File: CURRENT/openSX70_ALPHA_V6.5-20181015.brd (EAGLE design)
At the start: 95.9 x 27.9 mm, 42 parts, among them J1 687106183722, Q1 5.8A/30V/35mΩ, Q2 5.8A/30V/35mΩ, U1 ATMEGA328P_TQFP, Y1 CSTCE8M00G52Z-R0

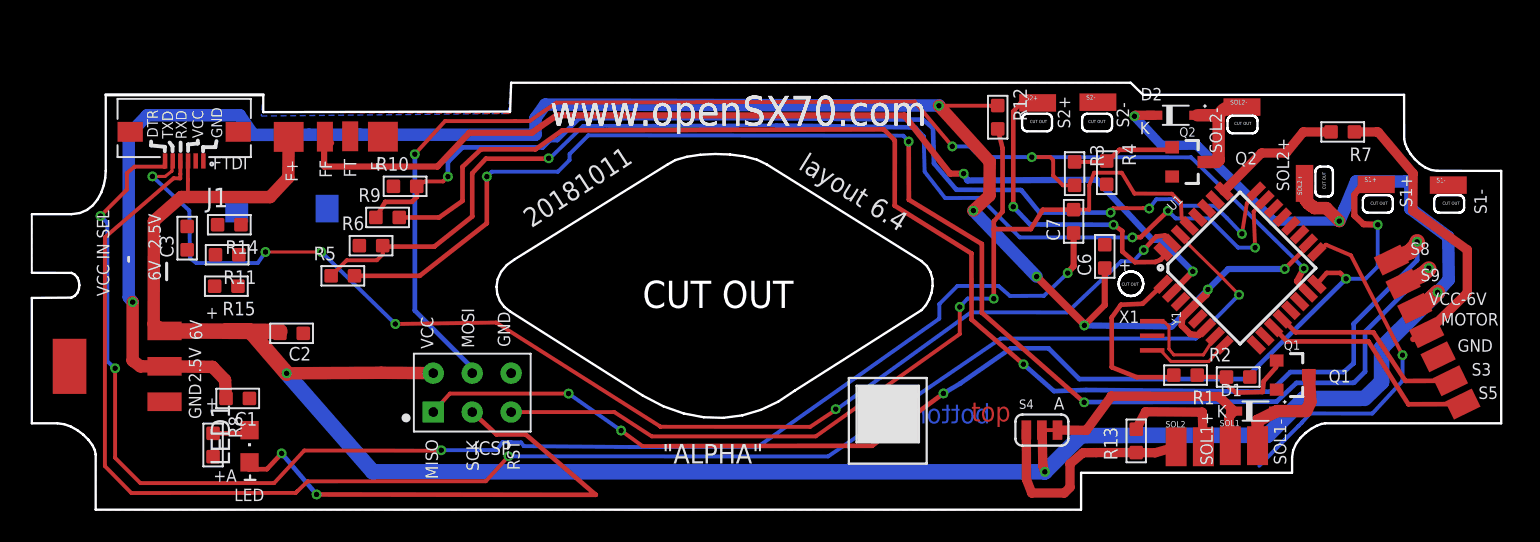
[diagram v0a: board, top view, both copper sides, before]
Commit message: New layout 6.5 with new flexcable custom connector
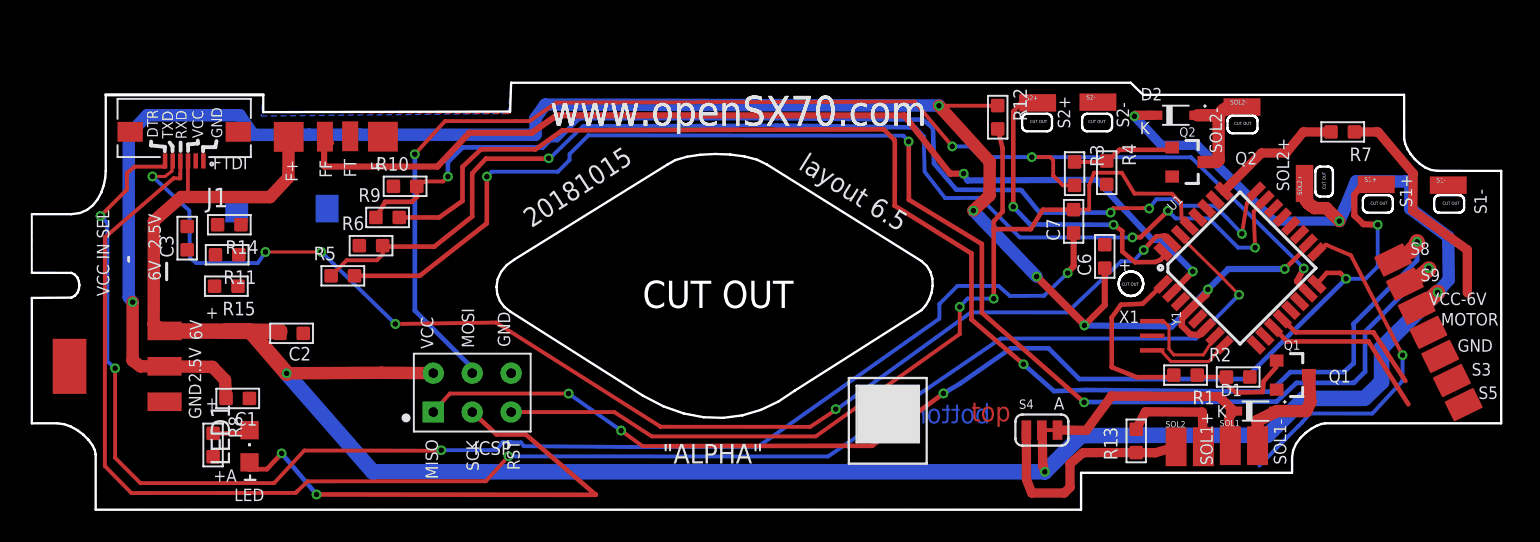
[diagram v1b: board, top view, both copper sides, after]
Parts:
- removed U$1: SX70-7-PAD, openSX70:SX70-7-PAD
- added U$3: SX70-7-PAD, _openSX70:SX70-7-PAD-PROPER
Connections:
- net 6V: now also U$3.VCC; no longer U$1.VCC-6V
- net GND: now also U$3.GND; no longer U$1.GND
- net MOTOR-HEADER: now also U$3.MOTOR; no longer U$1.MOTOR+
- net S3: now also U$3.S3; no longer U$1.S3
- net S5: now also U$3.S5; no longer U$1.S5
- net S8@6V: now also U$3.S8; no longer U$1.S8
- net S9@6V: now also U$3.S9; no longer U$1.S9
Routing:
- net MOTOR-HEADER: track 19.4 -> 14.7 mm
- net S5: track 15.8 -> 11.4 mm
- net S3: track 13.0 -> 10.1 mm
- net S9@6V: track 94.3 -> 92.9 mm
- net S8@6V: track 89.7 -> 88.4 mm
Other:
- board text added: "20181015"
- board text added: "layout 6.5"
- board text added: "openSX70 project visit www.openSX70.com version 6.5 "ALPHA" 20181015 by Joaquín de Prada"
- board text removed: "20181011"
- board text removed: "layout 6.4"
- board text removed: "openSX70 project visit www.openSX70.com version 6.4 "ALPHA" 20181011 by Joaquín de Prada"

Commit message: adding to the board
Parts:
- added LED2: DUAL-LED-3MM-NO-HOLE, _openSX70:DUOLED-A-3MM
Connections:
- new net LED2: LED2.ANODE-GREEN, U1.9
- net LED: now also LED2.ANODE-RED
- net N$5: now also LED2.COMMON-CATODE
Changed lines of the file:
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@@
 <grid distance="0.005" unitdist="mm" unit="mm" style="lines" multiple="1" display="yes" altdistance="0.0005" altunitdist="mm" altunit="mm"/>
 <layers>
-<layer number="1" name="Top" color="4" fill="1" visible="yes" active="yes"/>
+<layer number="1" name="Top" color="4" fill="1" visible="no" active="yes"/>
 <layer number="2" name="Route2" color="1" fill="3" visible="no" active="no"/>
 <layer number="3" name="Route3" color="4" fill="3" visible="no" active="no"/>
@@
 <layer number="19" name="Unrouted" color="6" fill="1" visible="yes" active="yes"/>
 <layer number="20" name="Dimension" color="24" fill="1" visible="yes" active="yes"/>
-<layer number="21" name="tPlace" color="7" fill="1" visible="yes" active="yes"/>
+<layer number="21" name="tPlace" color="7" fill="1" visible="no" active="yes"/>
 <layer number="22" name="bPlace" color="7" fill="1" visible="yes" active="yes"/>
-<layer number="23" name="tOrigins" color="15" fill="1" visible="yes" active="yes"/>
+<layer number="23" name="tOrigins" color="15" fill="1" visible="no" active="yes"/>
 <layer number="24" name="bOrigins" color="15" fill="1" visible="yes" active="yes"/>
-<layer number="25" name="tNames" color="7" fill="1" visible="yes" active="yes"/>
+<layer number="25" name="tNames" color="7" fill="1" visible="no" active="yes"/>
 <layer number="26" name="bNames" color="7" fill="1" visible="yes" active="yes"/>
 <layer number="27" name="tValues" color="7" fill="1" visible="no" active="yes"/>
@@
 <layer number="37" name="tTest" color="7" fill="1" visible="no" active="yes"/>
 <layer number="38" name="bTest" color="7" fill="1" visible="no" active="yes"/>
-<layer number="39" name="tKeepout" color="4" fill="11" visible="yes" active="yes"/>
+<layer number="39" name="tKeepout" color="4" fill="11" visible="no" active="yes"/>
 <layer number="40" name="bKeepout" color="1" fill="11" visible="yes" active="yes"/>
-<layer number="41" name="tRestrict" color="4" fill="10" visible="yes" active="yes"/>
+<layer number="41" name="tRestrict" color="4" fill="10" visible="no" active="yes"/>
 <layer number="42" name="bRestrict" color="1" fill="10" visible="yes" active="yes"/>
 <layer number="43" name="vRestrict" color="2" fill="10" visible="no" active="yes"/>
-<layer number="44" name="Drills" color="7" fill="1" visible="yes" active="yes"/>
+<layer number="44" name="Drills" color="7" fill="1" visible="no" active="yes"/>
 <layer number="45" name="Holes" color="7" fill="1" visible="yes" active="yes"/>
 <layer number="46" name="Milling" color="3" fill="1" visible="no" active="yes"/>
@@
 <layer number="49" name="Reference" color="7" fill="1" visible="no" active="yes"/>
 <layer number="50" name="dxf" color="7" fill="1" visible="no" active="no"/>
-<layer number="51" name="tDocu" color="7" fill="1" visible="yes" active="yes"/>
+<layer number="51" name="tDocu" color="7" fill="1" visible="no" active="yes"/>
 <layer number="52" name="bDocu" color="7" fill="1" visible="yes" active="yes"/>
 <layer number="53" name="tGND_GNDA" color="7" fill="9" visible="no" active="no"/>
@@
 <element name="C1" library="Seeed-Capacitor" library_urn="urn:adsk.eagle:library:464" package="C0603" package3d_urn="urn:adsk.eagle:package:32378/1" value="10uf" x="15.494" y="8.0645" rot="R270">
 <attribute name="MPN" value="CC0603KRX5R6BB106" x="15.494" y="8.0645" size="1.778" layer="27" rot="R270" display="off"/>
+<attribute name="NAME" x="16.764" y="8.3185" size="0.635" layer="33" ratio="10" rot="R180"/>
 <attribute name="NAME" x="16.764" y="7.1755" size="0.889" layer="25" ratio="11" rot="R180"/>
-<attribute name="NAME" x="16.764" y="8.3185" size="0.635" layer="33" ratio="10" rot="R180"/>
 <attribute name="VALUE" x="16.764" y="9.652" size="0.635" layer="27" ratio="10" rot="R180"/>
 </element>
 <element name="C2" library="Seeed-Capacitor" library_urn="urn:adsk.eagle:library:464" package="C0603" package3d_urn="urn:adsk.eagle:package:32378/1" value="100nf" x="19.009" y="12.3135" rot="R270">
 <attribute name="MPN" value="CC0603KRX7R9BB104" x="19.009" y="12.3135" size="1.778" layer="27" rot="R270" display="off"/>
+<attribute name="NAME" x="20.279" y="12.5675" size="0.635" layer="33" ratio="10" rot="R180"/>
 <attribute name="NAME" x="20.279" y="11.4245" size="0.889" layer="25" ratio="11" rot="R180"/>
-<attribute name="NAME" x="20.279" y="12.5675" size="0.635" layer="33" ratio="10" rot="R180"/>
 <attribute name="VALUE" x="20.279" y="13.901" size="0.635" layer="27" ratio="10" rot="R180"/>
 </element>
 <element name="C6" library="Seeed-Capacitor" library_urn="urn:adsk.eagle:library:464" package="C0603" package3d_urn="urn:adsk.eagle:package:32378/1" value="100nf" x="72.0725" y="17.3355" rot="R180">
 <attribute name="MPN" value="CC0603KRX7R9BB104" x="72.0725" y="17.3355" size="1.778" layer="27" rot="R180" display="off"/>
+<attribute name="NAME" x="72.3265" y="16.0655" size="0.635" layer="33" ratio="10" rot="R90"/>
 <attribute name="NAME" x="71.1835" y="16.0655" size="0.889" layer="25" ratio="11" rot="R90"/>
-<attribute name="NAME" x="72.3265" y="16.0655" size="0.635" layer="33" ratio="10" rot="R90"/>
 <attribute name="VALUE" x="73.66" y="16.0655" size="0.635" layer="27" ratio="10" rot="R90"/>
 </element>
 <element name="C7" library="Seeed-Capacitor" library_urn="urn:adsk.eagle:library:464" package="C0603" package3d_urn="urn:adsk.eagle:package:32378/1" value="100nf" x="70.0405" y="19.6215" rot="R180">
 <attribute name="MPN" value="CC0603KRX7R9BB104" x="70.0405" y="19.6215" size="1.778" layer="27" rot="R180" display="off"/>
+<attribute name="NAME" x="70.2945" y="18.3515" size="0.635" layer="33" ratio="10" rot="R90"/>
 <attribute name="NAME" x="69.1515" y="18.3515" size="0.889" layer="25" ratio="11" rot="R90"/>
-<attribute name="NAME" x="70.2945" y="18.3515" size="0.635" layer="33" ratio="10" rot="R90"/>
 <attribute name="VALUE" x="71.628" y="18.3515" size="0.635" layer="27" ratio="10" rot="R90"/>
 </element>
@@
 <element name="C3" library="Seeed-Capacitor" library_urn="urn:adsk.eagle:library:464" package="C0603" package3d_urn="urn:adsk.eagle:package:32378/1" value="100nf" x="12.195" y="18.525" rot="R180">
 <attribute name="MPN" value="CC0603KRX7R9BB104" x="12.195" y="18.525" size="1.778" layer="27" rot="R180" display="off"/>
+<attribute name="NAME" x="12.449" y="17.255" size="0.635" layer="33" ratio="10" rot="R90"/>
 <attribute name="NAME" x="11.306" y="17.255" size="0.889" layer="25" ratio="11" rot="R90"/>
-<attribute name="NAME" x="12.449" y="17.255" size="0.635" layer="33" ratio="10" rot="R90"/>
 <attribute name="VALUE" x="13.7825" y="17.255" size="0.635" layer="27" ratio="10" rot="R90"/>
 </element>
@@
 </element>
 <element name="U$3" library="_openSX70" package="SX70-7-PAD-PROPER" value="SX70-7-PAD" x="89.23" y="17.261" rot="R296"/>
+<element name="LED2" library="_openSX70" package="DUOLED-A-3MM" package3d_urn="urn:adsk.eagle:package:15877/1" value="DUAL-LED-3MM-NO-HOLE" x="29.6" y="30.065" rot="MR180">
+<attribute name="NAME" x="33.41" y="27.525" size="1.27" layer="26" ratio="10" rot="MR180"/>
+<attribute name="VALUE" x="33.41" y="32.605" size="1.27" layer="28" ratio="10" rot="MR180"/>
+</element>
 </elements>
 <signals>
@@
 <wire x1="91.5035" y1="9.2075" x2="91.5035" y2="10.89025" width="0.254" layer="16"/>
 <via x="18.3618" y="4.4832" extent="1-16" drill="0.35"/>
+<contactref element="LED2" pad="ANODE-RED"/>
 <wire x1="38.861665625" y1="1.77511875" x2="82.1569" y2="3.6709" width="0" layer="19" extent="1-16"/>
+<wire x1="27.1" y1="30.065" x2="16.215" y2="3.435" width="0" layer="19" extent="1-1"/>
 </signal>
 <signal name="S3">
@@
 <contactref element="R8" pad="2"/>
 <contactref element="LED1" pad="C"/>
-<wire x1="13.885" y1="5.788" x2="15.15" y2="5.788" width="0.3048" layer="1"/>
-<wire x1="15.15" y1="5.788" x2="16.058" y2="5.788" width="0.3048" layer="1"/>
+<wire x1="13.885" y1="5.788" x2="16.058" y2="5.788" width="0.3048" layer="1"/>
 <wire x1="16.058" y1="5.788" x2="16.265" y2="5.995" width="0.3048" layer="1"/>
+<contactref element="LED2" pad="COMMON-CATODE"/>
+<wire x1="29.59" y1="30.065" x2="13.885" y2="5.788" width="0" layer="19" extent="1-1"/>
 </signal>
 <signal name="DTR">
@@
 <wire x1="15.707" y1="19.4" x2="83.085796875" y2="20.457353125" width="0" layer="19" extent="1-1"/>
 </signal>
+<signal name="LED2">
+<contactref element="LED2" pad="ANODE-GREEN"/>
+<contactref element="U1" pad="9"/>
+<wire x1="32.12" y1="30.065" x2="81.954425" y2="11.558271875" width="0" layer="19" extent="1-1"/>
+</signal>
 </signals>

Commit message: update
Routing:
- net S9@2.5V: track 75.7 -> 64.4 mm, vias 4 -> 3
- net S8@2.5V: track 69.5 -> 58.8 mm, vias 4 -> 3
- net S8@6V: track 88.4 -> 78.8 mm
- net S9@6V: track 92.9 -> 84.0 mm, vias 4 -> 3

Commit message: Work in progress
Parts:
- moved LED2 5.34 mm to (30.1, 24.7)
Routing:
- net SOL2: track 86.0 -> 52.8 mm, vias 4 -> 3
- net S8@6V: track 78.8 -> 49.4 mm
- net S9@6V: track 84.0 -> 73.4 mm
- net S9@2.5V: track 64.4 -> 57.9 mm
- net 3.3V: track 127.8 -> 122.3 mm
- net MOTOR-HEADER: track 14.7 -> 19.7 mm
- net S5: track 11.4 -> 15.5 mm
- net S3: track 10.1 -> 13.5 mm
- net 6V: track 174.1 -> 176.0 mm
- net S8@2.5V: track 58.8 -> 57.1 mm
- net TXD: track 81.7 -> 82.5 mm, vias 6 -> 4

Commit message: acccidentally modified?
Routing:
- net LED2: track 0.00 -> 84.7 mm, vias 0 -> 1
- net V1: track 0.00 -> 83.6 mm, vias 0 -> 6
- net V2-SDA: track 0.00 -> 82.4 mm, vias 0 -> 2
- net V3-SCL: track 0.00 -> 82.1 mm, vias 0 -> 8
- net PDIODE: track 0.00 -> 80.7 mm, vias 0 -> 5
- net LED: track 58.2 -> 132.2 mm, vias 3 -> 6
- net S2: track 20.6 -> 77.0 mm, vias 2 -> 4
- net S8@6V: track 49.4 -> 100.4 mm, vias 2 -> 4
- net N$5: track 2.47 -> 49.0 mm, vias 0 -> 1
- net SOL2: track 52.8 -> 77.0 mm, vias 3 -> 4
- net S9@6V: track 73.4 -> 93.9 mm, vias 3 -> 4
- net S9@2.5V: track 57.9 -> 75.9 mm, vias 3 -> 4
- net S8@2.5V: track 57.1 -> 70.9 mm, vias 3 -> 4
- net 3.3V: track 122.3 -> 126.8 mm
- net GND: track 0.00 -> 2.50 mm, vias 0 -> 18
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
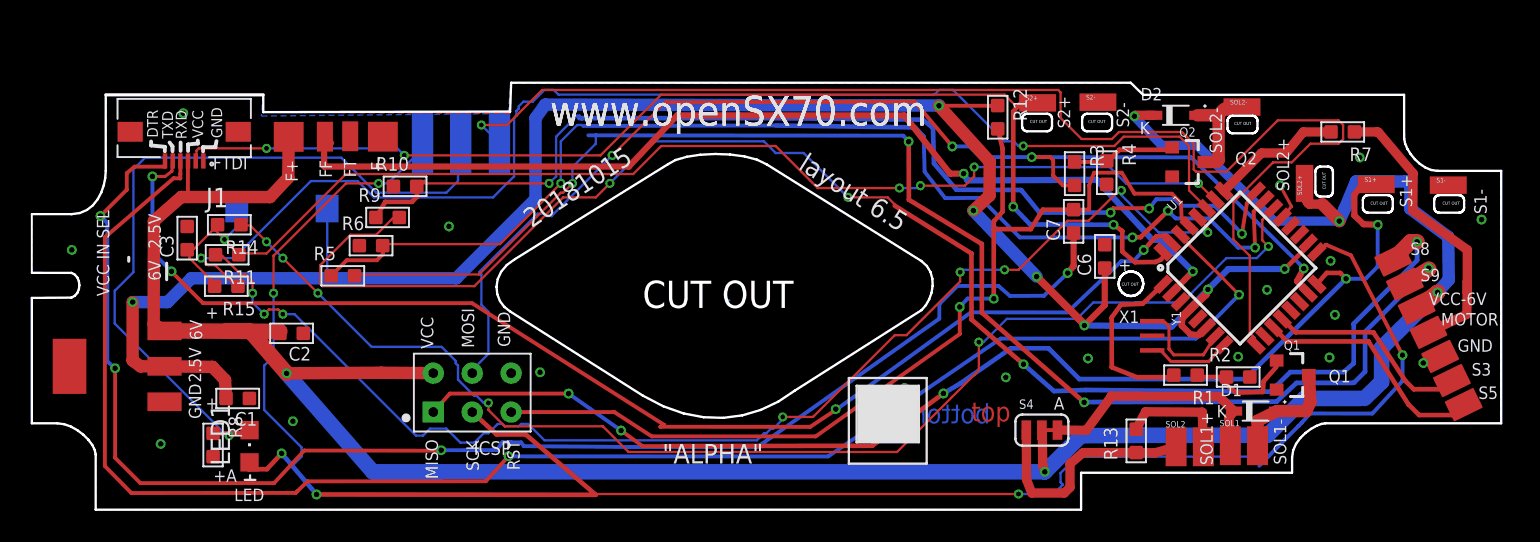
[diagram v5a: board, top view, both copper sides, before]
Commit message: new 7-pad (fixed the component) and WIP on the LED, new LED dual SMD
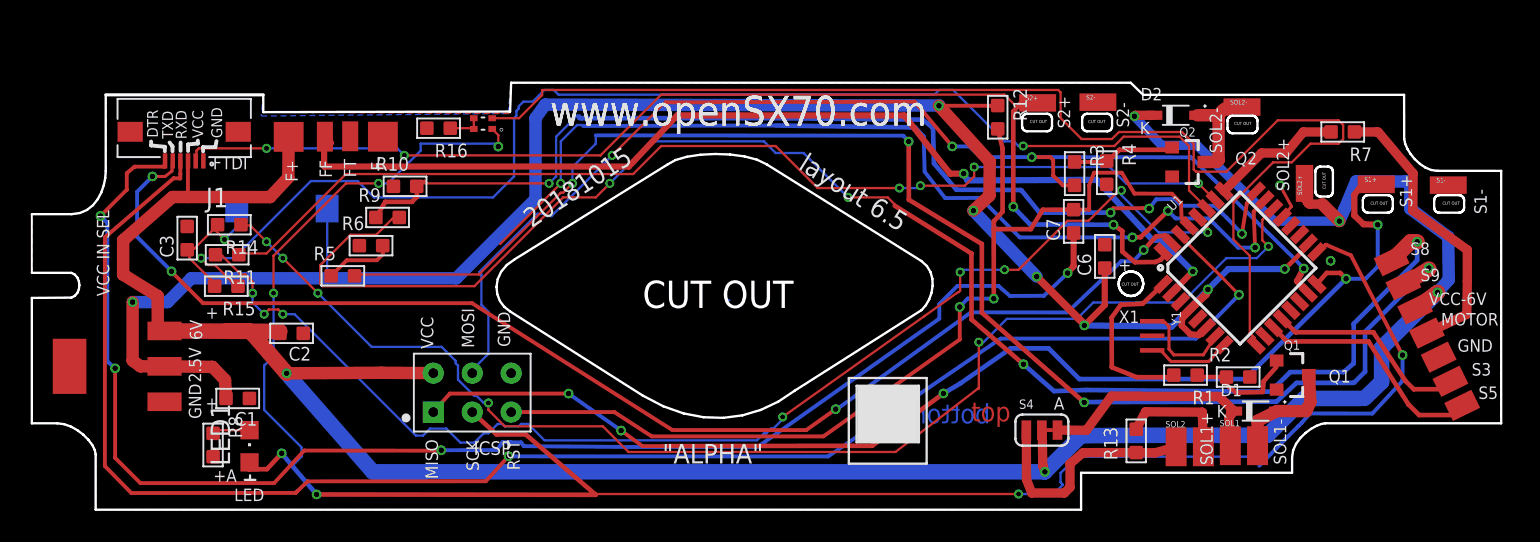
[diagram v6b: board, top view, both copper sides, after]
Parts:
- removed LED2: DUAL-LED-3MM-NO-HOLE, _openSX70:DUOLED-A-3MM
- added R16: 1K 1/10W, Seeed-Resistor:R0603
- added U$1: DUAL-LED-0603-BIS, _openSX70:LED_APHB1608SYKSURKC
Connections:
- new net N$9: R16.2, U$1.2, U$1.4
- net GND: now also R16.1
- net LED: now also U$1.1; no longer LED2.ANODE-RED
- net LED2: now also U$1.3; no longer LED2.ANODE-GREEN
- net N$5: no longer LED2.COMMON-CATODE
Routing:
- net N$5: track 49.0 -> 2.47 mm, vias 1 -> 0
- net S9@2.5V: track 75.9 -> 68.3 mm
- net LED: track 132.2 -> 138.5 mm, vias 6 -> 7
- net 6V: track 176.6 -> 172.8 mm
- net LED2: track 84.7 -> 82.3 mm, vias 1 -> 0
- net N$9: track 0.00 -> 2.26 mm
- net N$2: track 16.5 -> 15.4 mm
- net MOTOR-HEADER: track 19.7 -> 19.0 mm
- net GND: vias 18 -> 2
